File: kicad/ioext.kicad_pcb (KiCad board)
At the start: 2 copper layers, 70.1 x 60.2 mm, 46 parts, among them P1 CONN_01X04, P2 CONN_02X08, P3 CONN_01X10, Q1 IRLZ44N, Q2 IRLZ44N, Q3 IRLZ44N, Q4 IRLZ44N, Q5 IRLZ44N, Q6 IRLZ44N, Q7 IRLZ44N, Q8 IRLZ44N, U1 PCF8574A, U2 PC817, U3 PC817, U4 PC817, U5 PC817, U6 PC817, U7 PC817, U8 PC817, U9 PC817

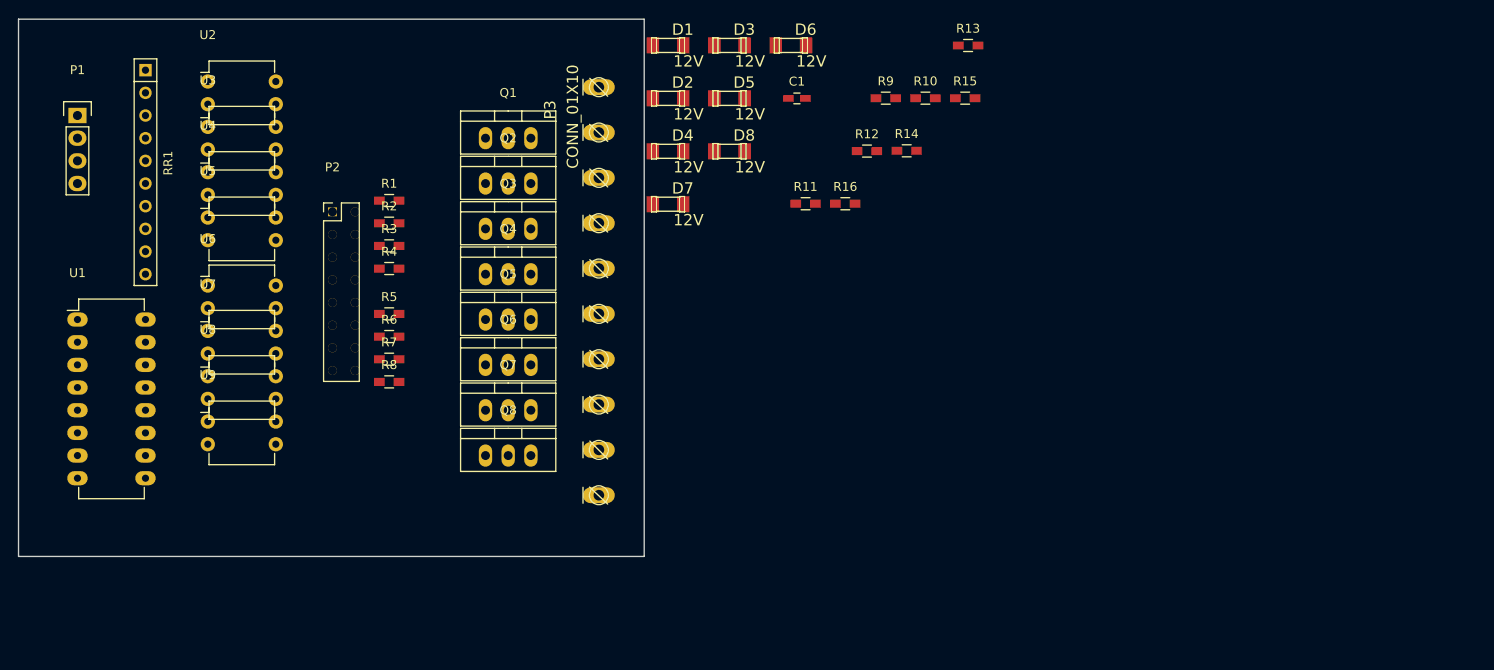
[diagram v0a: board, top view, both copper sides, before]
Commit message: kicad-ioext: components distributed
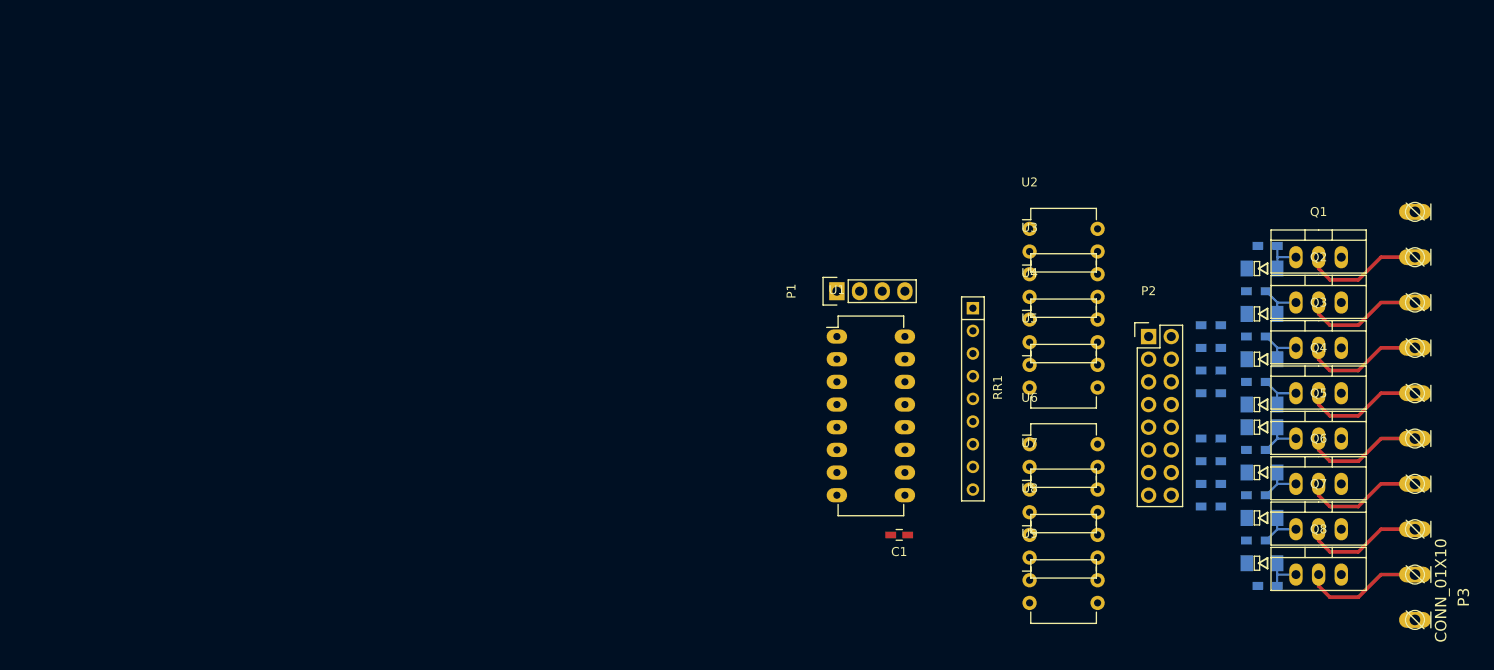
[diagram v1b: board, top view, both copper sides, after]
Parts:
- D1, D2, D3, D4, D5, D6, D7, D8, R1, R10, R11, R12, R13, R14, R15, R16, R2, R3, R4, R5, R6, R7, R8, R9: moved to B.Cu
- P2: footprint gate433:Pin_Header_Straight_2x08 -> Pin_Headers:Pin_Header_Straight_2x08
- RR1: footprint Resistors_ThroughHole:Resistor_Array_SIP9 -> Resistors_ThroughHole:Resistor_Array_SIP8
- moved RR1 96.1 mm to (219.7, 109.9)
- moved U9 93.8 mm to (226.1, 130.2)
- moved U6 93.8 mm to (226.1, 114.9)
- moved U7 93.8 mm to (226.1, 120.0)
- moved U8 93.8 mm to (226.1, 125.1)
- moved U2 93.5 mm to (226.1, 90.8)
- moved U3 93.5 mm to (226.1, 95.9)
- moved U4 93.5 mm to (226.1, 101.0)
- moved U5 93.5 mm to (226.1, 106.0)
- moved R1 93.1 mm to (246.4, 101.6), turned to 180 degrees
- moved R2 93.1 mm to (246.4, 104.1), turned to 180 degrees
- moved R3 93.1 mm to (246.4, 106.7), turned to 180 degrees
- moved R4 93.1 mm to (246.4, 109.2), turned to 180 degrees
- moved R5 93.1 mm to (246.4, 114.3), turned to 180 degrees
- moved R6 93.1 mm to (246.4, 116.8), turned to 180 degrees
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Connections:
- net Net-(C1-Pad1) renamed +5V
- net Net-(C1-Pad2) renamed GND
- D1 pad 2: Net-(D1-Pad2) -> GNDA
- D2 pad 2: Net-(D1-Pad2) -> GNDA
- D3 pad 2: Net-(D1-Pad2) -> GNDA
- D4 pad 2: Net-(D1-Pad2) -> GNDA
- D5 pad 2: Net-(D1-Pad2) -> GNDA
- D7 pad 2: Net-(D1-Pad2) -> GNDA
- D8 pad 2: Net-(D1-Pad2) -> GNDA
- P3 pad 1: Net-(D1-Pad2) -> +12V
- P3 pad 10: +12V -> GNDA
- Q1 pad 2: Net-(P3-Pad2) -> Net-(P3-Pad9)
- Q1 pad 3: Net-(D1-Pad2) -> GNDA
- Q2 pad 2: Net-(P3-Pad3) -> Net-(P3-Pad8)
- Q2 pad 3: Net-(D1-Pad2) -> GNDA
- Q3 pad 2: Net-(P3-Pad4) -> Net-(P3-Pad7)
- Q3 pad 3: Net-(D1-Pad2) -> GNDA
- Q4 pad 2: Net-(P3-Pad5) -> Net-(P3-Pad6)
- Q4 pad 3: Net-(D1-Pad2) -> GNDA
- Q5 pad 2: Net-(P3-Pad6) -> Net-(P3-Pad5)
- Q5 pad 3: Net-(D1-Pad2) -> GNDA
- Q6 pad 2: Net-(P3-Pad7) -> Net-(P3-Pad4)
- Q6 pad 3: Net-(D6-Pad2) -> GNDA
- Q7 pad 2: Net-(P3-Pad8) -> Net-(P3-Pad3)
- Q7 pad 3: Net-(D1-Pad2) -> GNDA
- Q8 pad 2: Net-(P3-Pad9) -> Net-(P3-Pad2)
- Q8 pad 3: Net-(D1-Pad2) -> GNDA
- R10 pad 2: Net-(D1-Pad2) -> GNDA
- R11 pad 2: Net-(D1-Pad2) -> GNDA
- R12 pad 2: Net-(D1-Pad2) -> GNDA
- R13 pad 2: Net-(D1-Pad2) -> GNDA
- R14 pad 2: Net-(D6-Pad2) -> Net-(R14-Pad2)
- R15 pad 2: Net-(D1-Pad2) -> GNDA
- R16 pad 2: Net-(D1-Pad2) -> GNDA
- R9 pad 2: Net-(D1-Pad2) -> GNDA
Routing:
- net Net-(P3-Pad2): track 0.00 -> 13.6 mm
- net Net-(P3-Pad4): track 0.00 -> 13.6 mm
- net Net-(P3-Pad3): track 0.00 -> 13.6 mm
- net Net-(P3-Pad7): track 0.00 -> 13.6 mm
- net Net-(P3-Pad6): track 0.00 -> 13.6 mm
- net Net-(P3-Pad5): track 0.00 -> 13.6 mm
- net Net-(P3-Pad9): track 0.00 -> 13.6 mm
- net Net-(P3-Pad8): track 0.00 -> 13.6 mm
- net Net-(D7-Pad1): track 0.00 -> 5.18 mm
- net Net-(D6-Pad1): track 0.00 -> 5.18 mm
- net Net-(D5-Pad1): track 0.00 -> 5.18 mm
- net Net-(D4-Pad1): track 0.00 -> 5.16 mm
- net Net-(D3-Pad1): track 0.00 -> 5.16 mm
- net Net-(D2-Pad1): track 0.00 -> 5.16 mm
- net Net-(D8-Pad1): track 0.00 -> 4.67 mm
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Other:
- board outline removed
- net class Power added: clearance 0.25, trace_width 0.4, via_dia 1, via_drill 0.6

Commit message: kicad-ioext: wiring
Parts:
- added A: MountingHole_3.2mm_M3, Mounting_Holes:MountingHole_3.2mm_M3, F.Cu at (213.2, 91.8)
- added B: MountingHole_3.2mm_M3, Mounting_Holes:MountingHole_3.2mm_M3, F.Cu at (246.2, 91.8)
- added C: MountingHole_3.2mm_M3, Mounting_Holes:MountingHole_3.2mm_M3, F.Cu at (213.2, 131.8)
- added D: MountingHole_3.2mm_M3, Mounting_Holes:MountingHole_3.2mm_M3, F.Cu at (246.2, 131.8)
- C1: moved to B.Cu
- moved P1 14.0 mm to (218.4, 98.4), turned to 270 degrees
- moved U1 6.35 mm to (210.8, 102.9)
- moved C1 4.49 mm to (215.9, 125.7)
- moved RR1 2.01 mm to (221.6, 110.5)
- moved U2 0.63 mm to (226.7, 90.8)
- moved U3 0.63 mm to (226.7, 95.9)
- moved U4 0.63 mm to (226.7, 101.0)
- moved U5 0.63 mm to (226.7, 106.0)
- moved U6 0.63 mm to (226.7, 114.9)
- moved U7 0.63 mm to (226.7, 120.0)
- moved U8 0.63 mm to (226.7, 125.1)
- moved U9 0.63 mm to (226.7, 130.2)
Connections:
- D6 pad 2: Net-(D6-Pad2) -> GNDA
- Q6 pad 3: GNDA -> Net-(Q6-Pad3)
- R14 pad 2: Net-(R14-Pad2) -> GNDA
- U1 pad 14: Net-(P1-Pad3) -> Net-(P1-Pad4)
- U1 pad 15: Net-(P1-Pad4) -> Net-(P1-Pad3)
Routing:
- net Net-(D8-Pad1): track 4.67 -> 42.4 mm
- net Net-(D1-Pad1): track 4.63 -> 38.7 mm
- net Net-(D7-Pad1): track 5.18 -> 37.1 mm
- net Net-(U1-Pad12): track 0.00 -> 31.5 mm
- net Net-(D2-Pad1): track 5.16 -> 34.9 mm
- net Net-(U1-Pad4): track 0.00 -> 28.2 mm
- net Net-(D6-Pad1): track 5.18 -> 33.1 mm
- net Net-(U1-Pad5): track 0.00 -> 27.1 mm
- net Net-(D3-Pad1): track 5.16 -> 30.8 mm
- net Net-(U1-Pad6): track 0.00 -> 25.3 mm
- net Net-(D5-Pad1): track 5.18 -> 29.5 mm
- net +12V: track 0.00 -> 23.3 mm, vias 0 -> 1
- net Net-(D4-Pad1): track 5.16 -> 28.1 mm
- net Net-(P2-Pad1): track 0.00 -> 22.8 mm
- net Net-(U1-Pad11): track 0.00 -> 22.6 mm
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- added copper zone on F.Cu, net +12V
- added copper zone on F.Cu, net +5V
- added copper zone on B.Cu, net GND
- added copper zone on B.Cu, net GNDA
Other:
- board outline added: 66 x 51 mm
- net class Default: trace_width 0.25 -> 0.254
- net class Power: trace_width 0.4 -> 0.6
